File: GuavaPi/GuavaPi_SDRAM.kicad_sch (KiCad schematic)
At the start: 7 parts, among them IC1 D2516ECMDXGJD-U, IC2 D2516ECMDXGJD-U

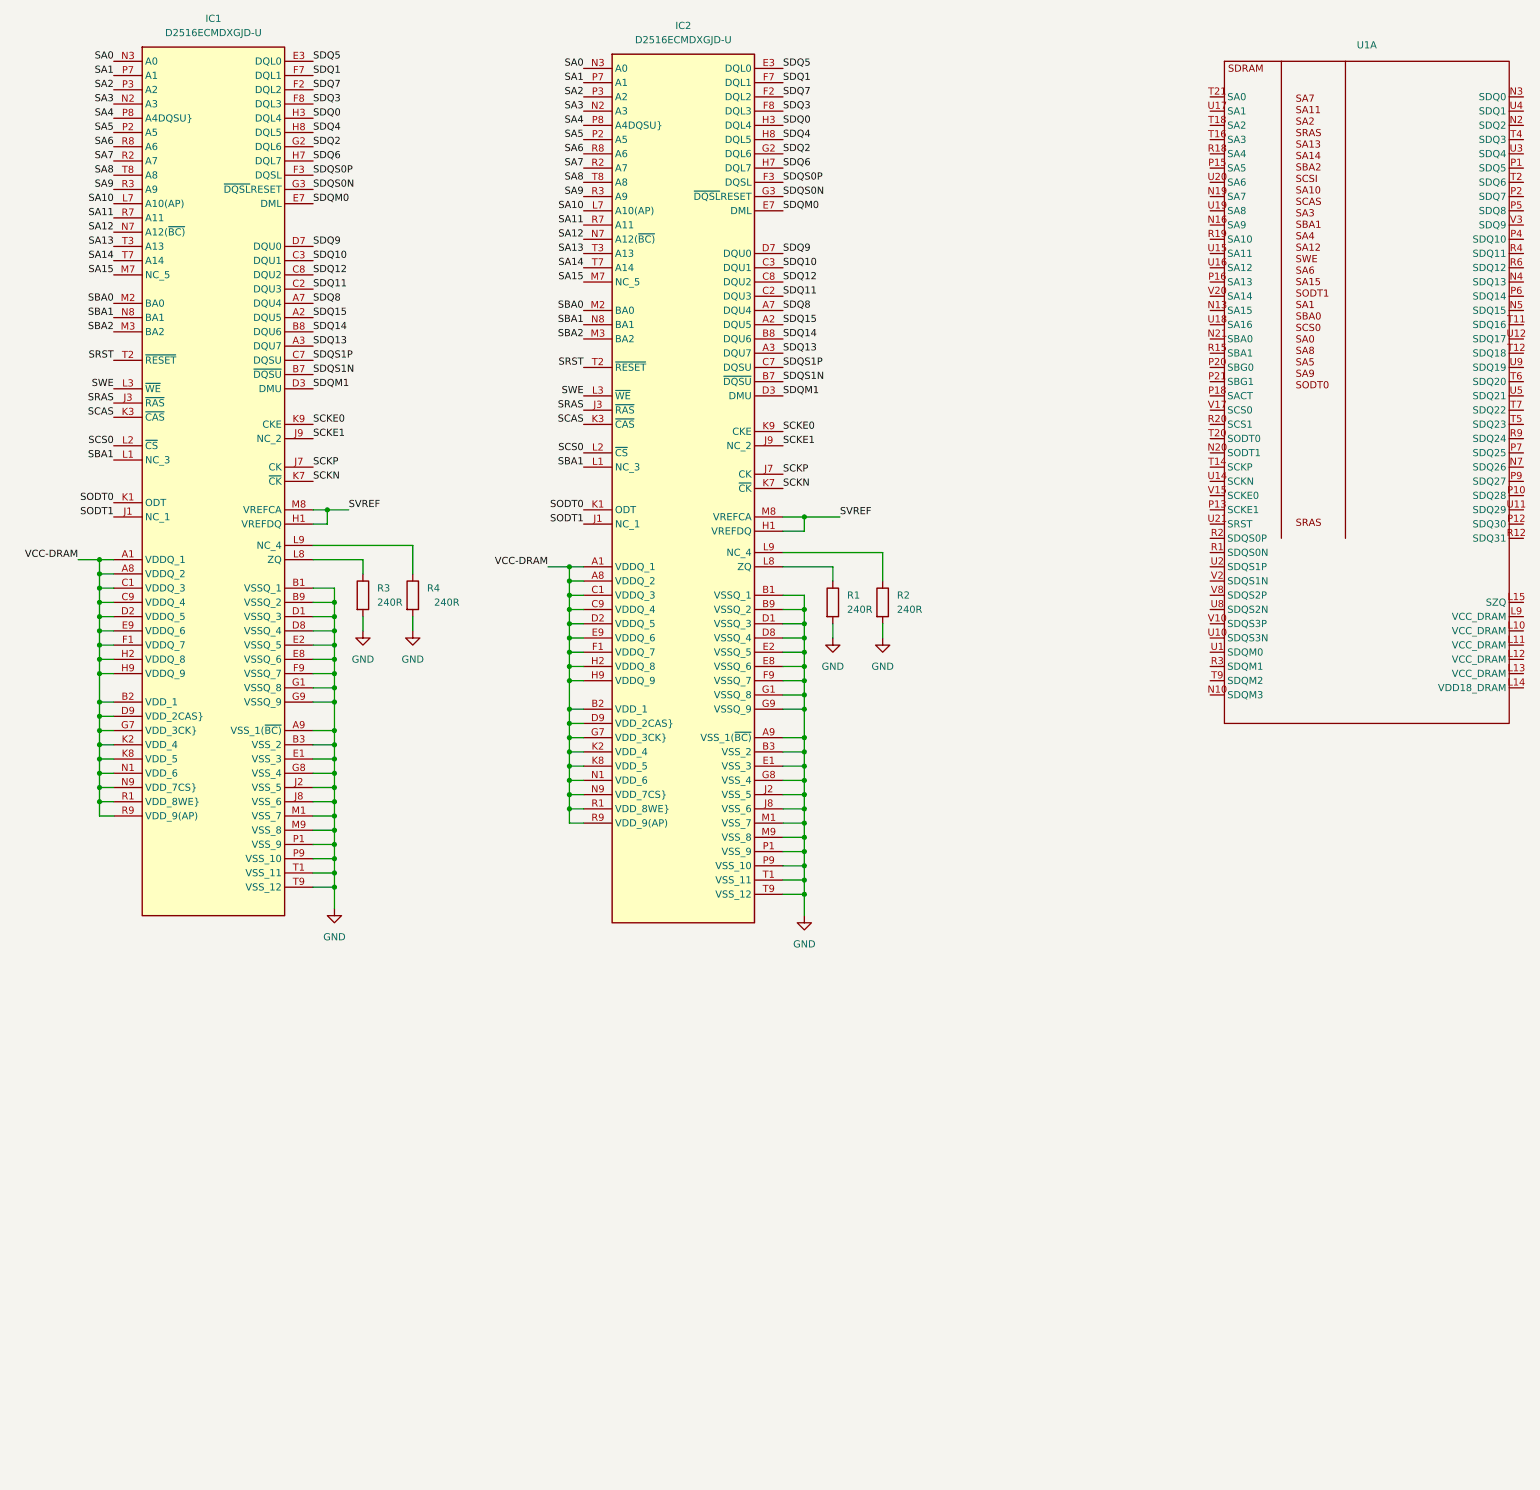
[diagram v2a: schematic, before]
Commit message: Completed SDRAM Section for H616
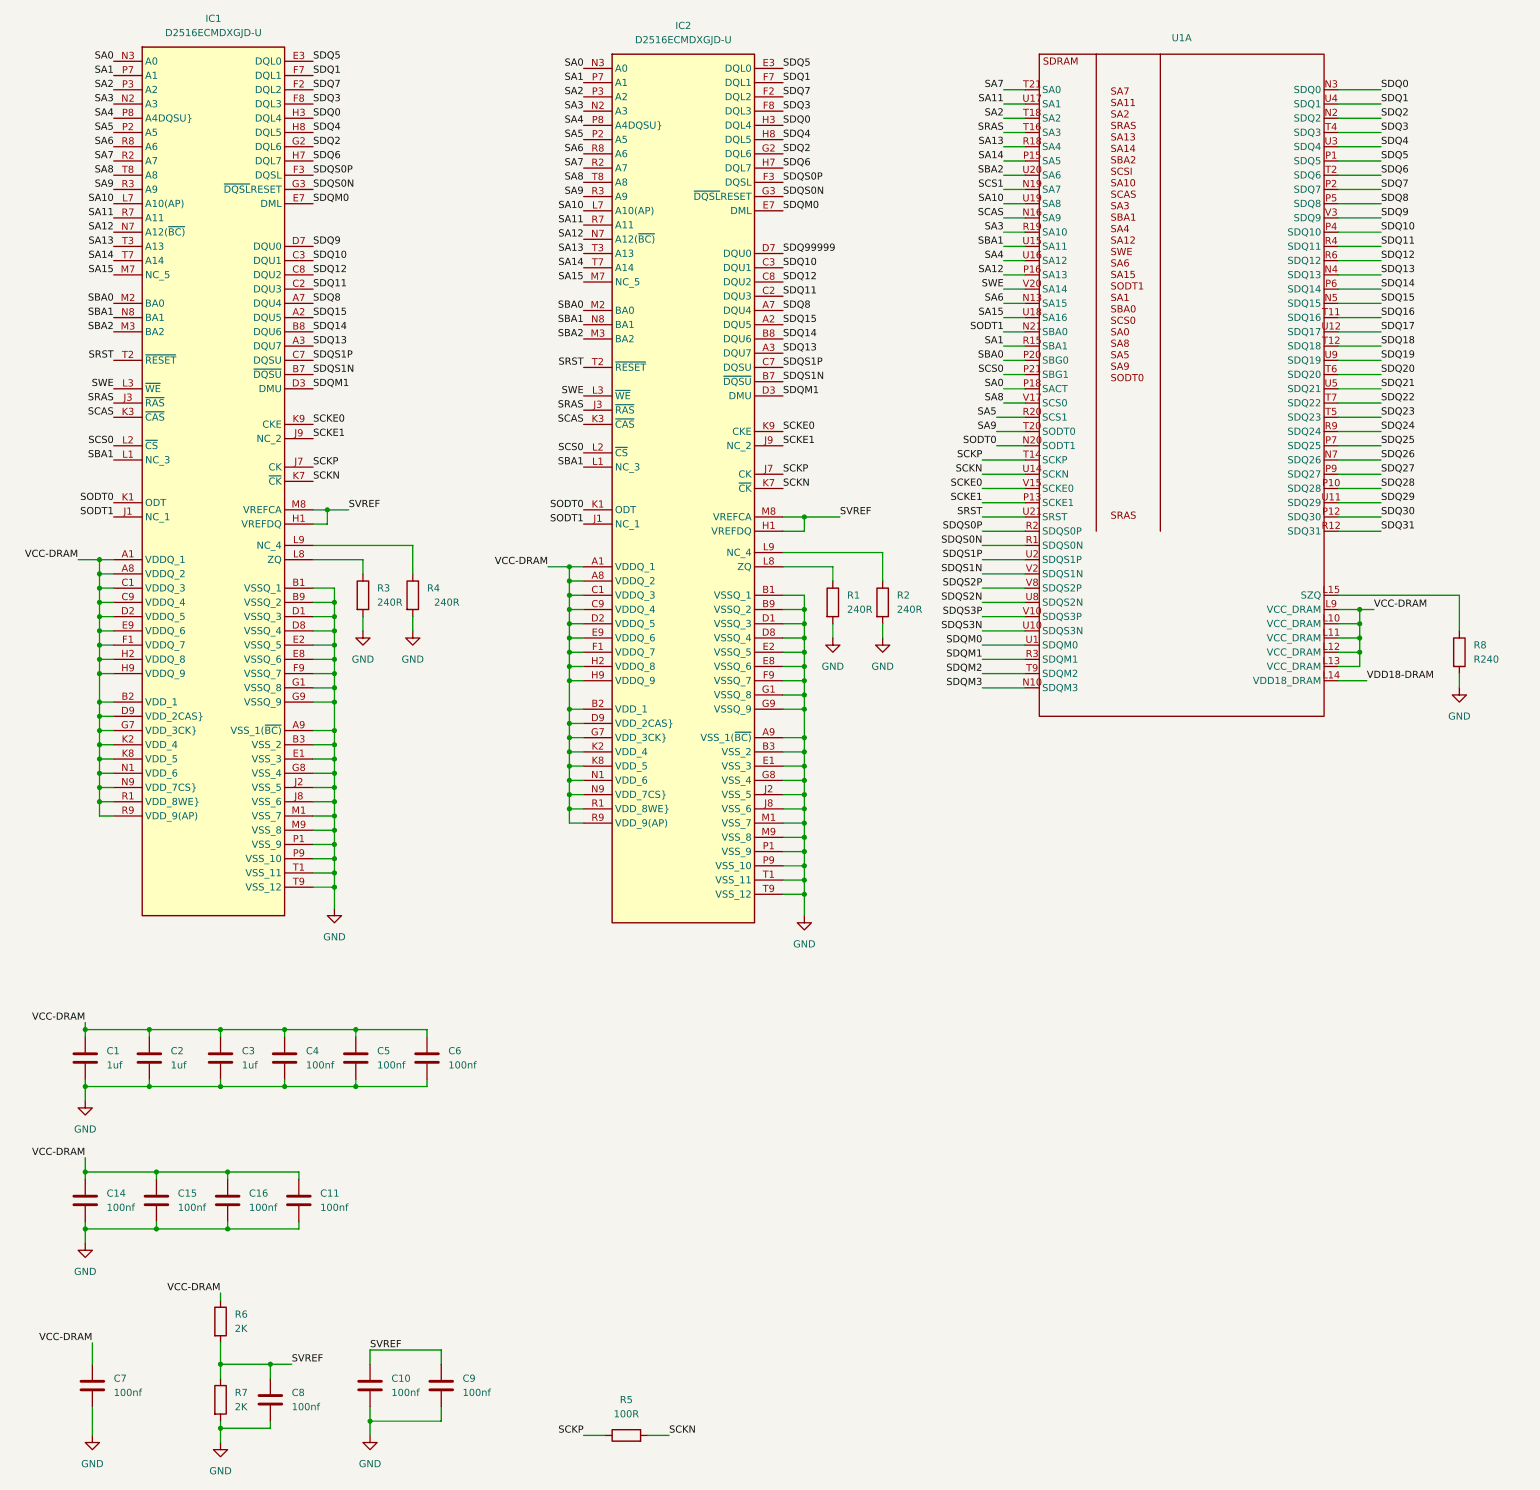
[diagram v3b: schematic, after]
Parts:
- added C1, C2, C3: 1uf, symbol Device:C
- added C10, C11, C14, C15, C16, C4, C5, C6, C7, C8, C9: 100nf, symbol Device:C
- added R5: 100R, symbol Device:R
- added R6, R7: 2K, symbol Device:R
- added R8: R240, symbol Device:R
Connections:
- net GND: now also C1.2, C10.2, C11.2, C14.2, C15.2, C16.2, C2.2, C3.2, C4.2, C5.2, C6.2, C7.2, C8.2, C9.2, R7.2, R8.2
- net SA0: now also U1.P18 (SACT)
- net SA1: now also U1.R15 (SBA1)
- net SA10: now also U1.U19 (SA8)
- net SA11: now also U1.U17 (SA1)
- net SA12: now also U1.P16 (SA13)
- net SA13: now also U1.R18 (SA4)
- net SA14: now also U1.P15 (SA5)
- net SA15: now also U1.U18 (SA16)
- net SA2: now also U1.T18 (SA2)
- net SA3: now also U1.R19 (SA10)
- net SA4: now also U1.U16 (SA12)
- net SA5: now also U1.R20 (SCS1)
- net SA6: now also U1.N13 (SA15)
- net SA7: now also U1.T21 (SA0)
- net SA8: now also U1.V17 (SCS0)
- net SA9: now also U1.T20 (SODT0)
- net SBA0: now also U1.P20 (SBG0)
- net SBA1: now also U1.U15 (SA11)
- net SBA2: now also U1.U20 (SA6)
- net SCAS: now also U1.N16 (SA9)
- net SCKE0: now also U1.V15 (SCKE0)
- net SCKE1: now also U1.P13 (SCKE1)
- net SCKN: now also U1.U14 (SCKN), R5.2
- net SCKP: now also U1.T14 (SCKP), R5.1
- net SCS0: now also U1.P21 (SBG1)
- net SDQ0: now also U1.N3 (SDQ0)
- net SDQ1: now also U1.U4 (SDQ1)
- net SDQ10: now also U1.P4 (SDQ10)
- net SDQ11: now also U1.R4 (SDQ11)
- net SDQ12: now also U1.R6 (SDQ12)
- net SDQ13: now also U1.N4 (SDQ13)
- net SDQ14: now also U1.P6 (SDQ14)
- net SDQ15: now also U1.N5 (SDQ15)
- net SDQ2: now also U1.N2 (SDQ2)
- net SDQ3: now also U1.T4 (SDQ3)
- net SDQ4: now also U1.U3 (SDQ4)
- net SDQ5: now also U1.P1 (SDQ5)
- net SDQ6: now also U1.T2 (SDQ6)
- net SDQ7: now also U1.P2 (SDQ7)
- net SDQ8: now also U1.P5 (SDQ8)
- net SDQ9: now also U1.V3 (SDQ9); no longer IC2.D7 (DQU0)
- net SDQM0: now also U1.U1 (SDQM0)
- net SDQM1: now also U1.R3 (SDQM1)
- net SDQS0N: now also U1.R1 (SDQS0N)
- net SDQS0P: now also U1.R2 (SDQS0P)
- net SDQS1N: now also U1.V2 (SDQS1N)
- net SDQS1P: now also U1.U2 (SDQS1P)
- net SODT0: now also U1.N20 (SODT1)
- net SODT1: now also U1.N21 (SBA0)
- net SRAS: now also U1.T16 (SA3)
- net SRST: now also U1.U21 (SRST)
- net SVREF: now also C10.1, C8.1, C9.1, R6.2, R7.1
- net SWE: now also U1.V20 (SA14)
- net VCC-DRAM: now also U1.L10 (VCC_DRAM), U1.L11 (VCC_DRAM), U1.L12 (VCC_DRAM), U1.L13 (VCC_DRAM), U1.L9 (VCC_DRAM), C1.1, C11.1, C14.1, C15.1, C16.1, C2.1, C3.1, C4.1, C5.1, C6.1, C7.1, R6.1
- net VDD18-DRAM: now reaches U1.L14 (VDD18_DRAM)
- net at U1.L15 (SZQ): now also R8.1
- net SDQM3: now reaches U1.N10 (SDQM3)
- net SCS1: now reaches U1.N19 (SA7)
- net SDQ26: now reaches U1.N7 (SDQ26)
- net SDQ28: now reaches U1.P10 (SDQ28)
- net SDQ30: now reaches U1.P12 (SDQ30)
- net SDQ25: now reaches U1.P7 (SDQ25)
- net SDQ27: now reaches U1.P9 (SDQ27)
- net SDQ31: now reaches U1.R12 (SDQ31)
- net SDQ24: now reaches U1.R9 (SDQ24)
- net SDQ16: now reaches U1.T11 (SDQ16)
- net SDQ18: now reaches U1.T12 (SDQ18)
- net SDQ23: now reaches U1.T5 (SDQ23)
- net SDQ20: now reaches U1.T6 (SDQ20)
- net SDQ22: now reaches U1.T7 (SDQ22)
- net SDQM2: now reaches U1.T9 (SDQM2)
- net SDQS3N: now reaches U1.U10 (SDQS3N)
- net SDQ29: now reaches U1.U11 (SDQ29)
- net SDQ17: now reaches U1.U12 (SDQ17)
- net SDQ21: now reaches U1.U5 (SDQ21)
- net SDQS2N: now reaches U1.U8 (SDQS2N)
- net SDQ19: now reaches U1.U9 (SDQ19)
- net SDQS3P: now reaches U1.V10 (SDQS3P)
- net SDQS2P: now reaches U1.V8 (SDQS2P)
- new net SDQ99999: IC2.D7 (DQU0)
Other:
- moved on the sheet: U1A

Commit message: Finished DDR3 Connections
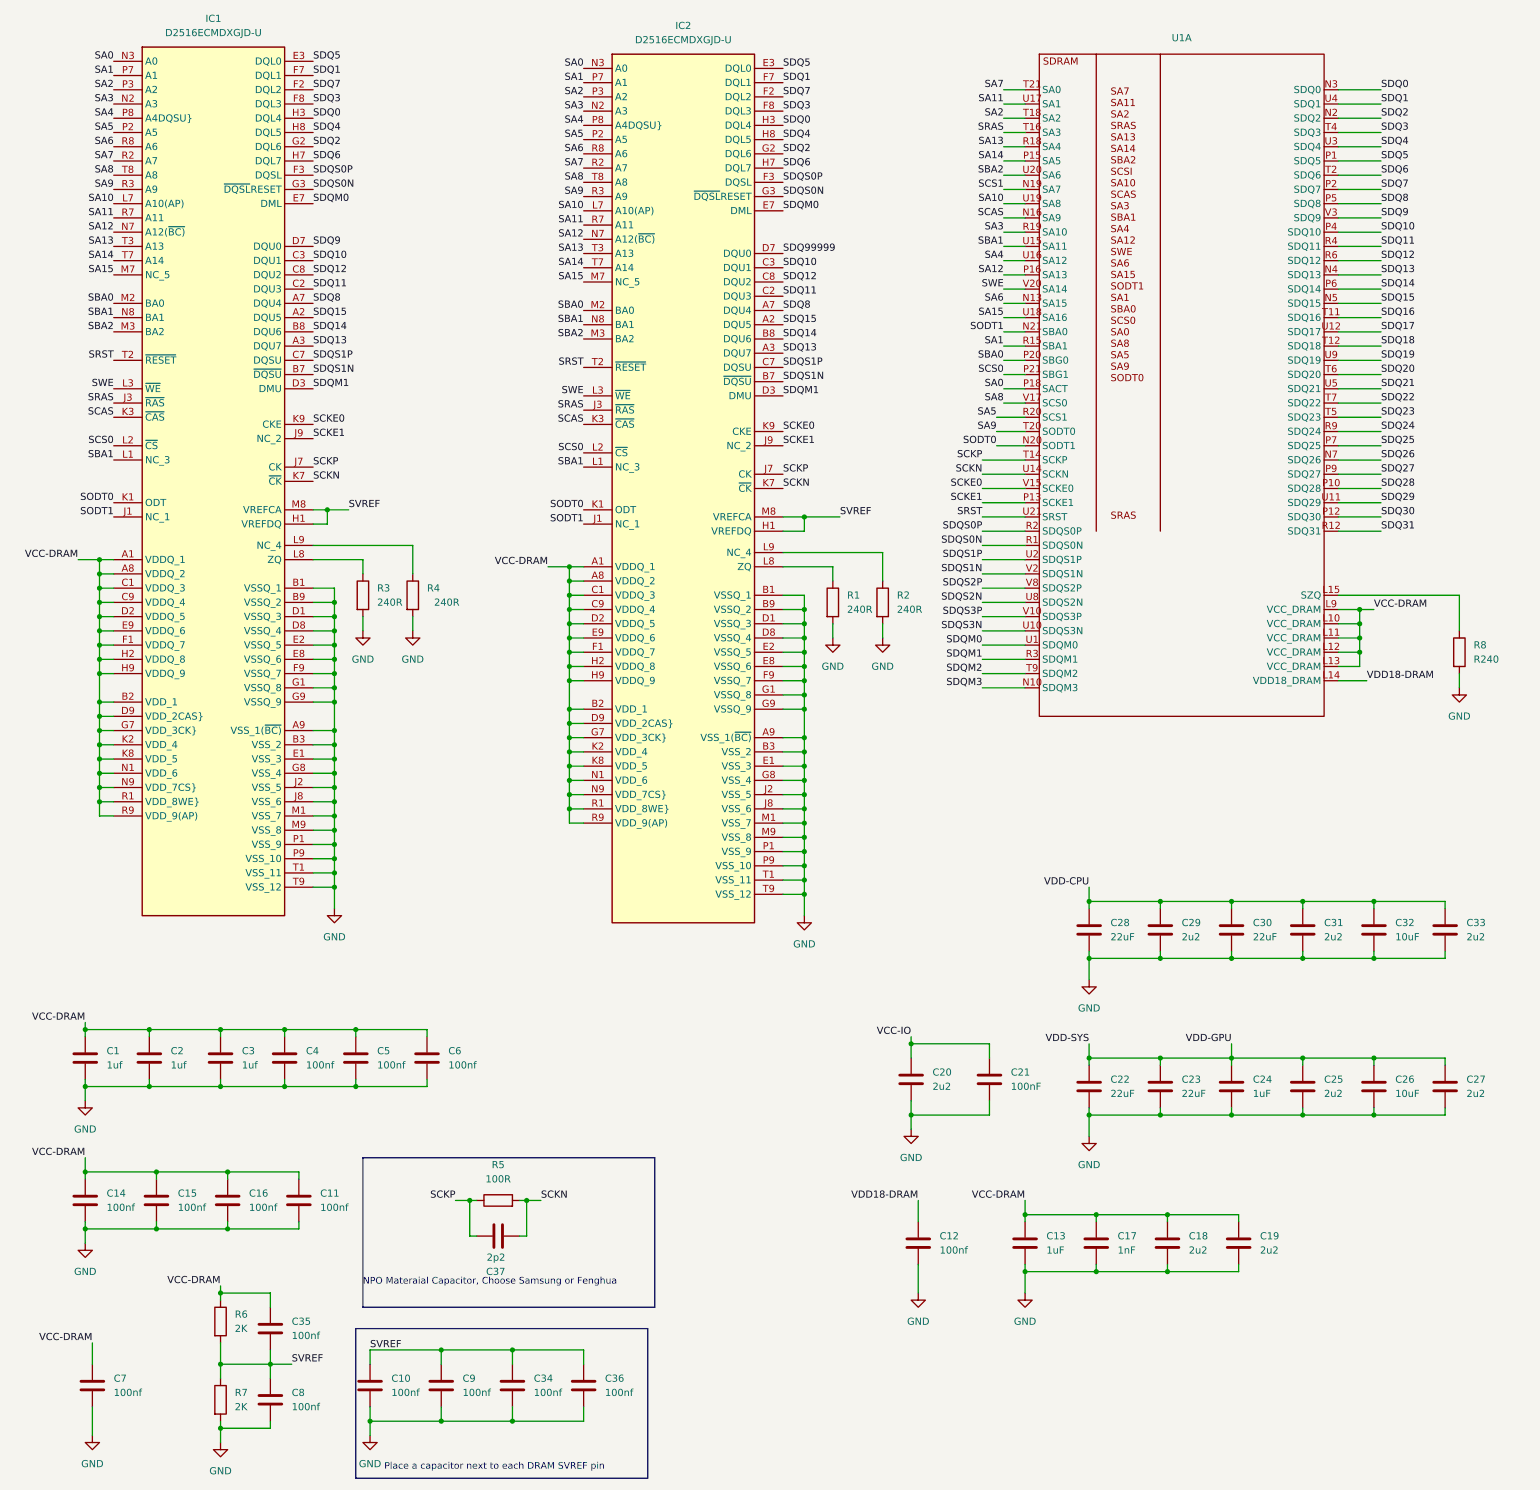
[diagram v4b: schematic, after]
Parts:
- added C12, C34, C35, C36: 100nf, symbol Device:C
- added C13, C24: 1uF, symbol Device:C
- added C17: 1nF, symbol Device:C
- added C18, C19, C20, C25, C27, C29, C31, C33: 2u2, symbol Device:C
- added C21: 100nF, symbol Device:C
- added C22, C23, C28, C30: 22uF, symbol Device:C
- added C26, C32: 10uF, symbol Device:C
- added C37: 2p2, symbol Device:C
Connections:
- net GND: now also C12.2, C13.2, C17.2, C18.2, C19.2, C20.2, C21.2, C22.2, C23.2, C24.2, C25.2, C26.2, C27.2, C28.2, C29.2, C30.2, C31.2, C32.2, C33.2, C34.2, C36.2
- net SCKN: now also C37.2
- net SCKP: now also C37.1
- net SVREF: now also C34.1, C35.2, C36.1
- net VCC-DRAM: now also C13.1, C17.1, C18.1, C19.1, C35.1
- net VDD18-DRAM: now also C12.1
- new net VCC-IO: C20.1, C21.1
- new net VDD-CPU: C28.1, C29.1, C30.1, C31.1, C32.1, C33.1
- new net VDD-GPU: C22.1, C23.1, C24.1, C25.1, C26.1, C27.1
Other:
- note added: "NPO Materaial Capacitor, Choose Samsung or Fenghua"
- note added: "Place a capacitor next to each DRAM SVREF pin"
- moved on the sheet: R5

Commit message: Misc
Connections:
- net SDQ99999 is gone; now on net SDQ9: IC2.D7 (DQU0)
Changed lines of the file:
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@@
     (effects (font (size 1.27 1.27)) (justify right bottom))
   )
-  (label "SDQ99999" (at 148.59 60.96 0) (fields_autoplaced)
+  (label "SDQ9" (at 148.59 60.96 0) (fields_autoplaced)
     (effects (font (size 1.27 1.27)) (justify left bottom))
   )
@@
     (pin "C20")
     (pin "D11")
+    (pin "D12")
     (pin "D13")
     (pin "D14")
@@
     (pin "B6")
     (pin "D10")
-    (pin "D12")
     (pin "D19")
-    (pin "F10")
     (pin "F10")
     (pin "F11")
@@
     (pin "F8")
     (pin "F9")
-    (pin "F9")
     (pin "G10")
     (pin "G11")
@@
     (pin "G15")
     (pin "G8")
-    (pin "G8")
-    (pin "G9")
     (pin "G9")
     (pin "H10")
@@
     (pin "L21")
     (pin "L8")
-    (pin "L8")
     (pin "M1")
     (pin "M2")
@@
           (reference "U1") (unit 1)
         )
+        (path "/3be7235b-2d12-456d-bbdb-dcc9c2ae1afd/0e09d813-5fde-42ce-9948-43290a465bd7"
+          (reference "U1") (unit 1)
+        )
